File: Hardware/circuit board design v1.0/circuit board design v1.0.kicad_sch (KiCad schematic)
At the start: 0 parts

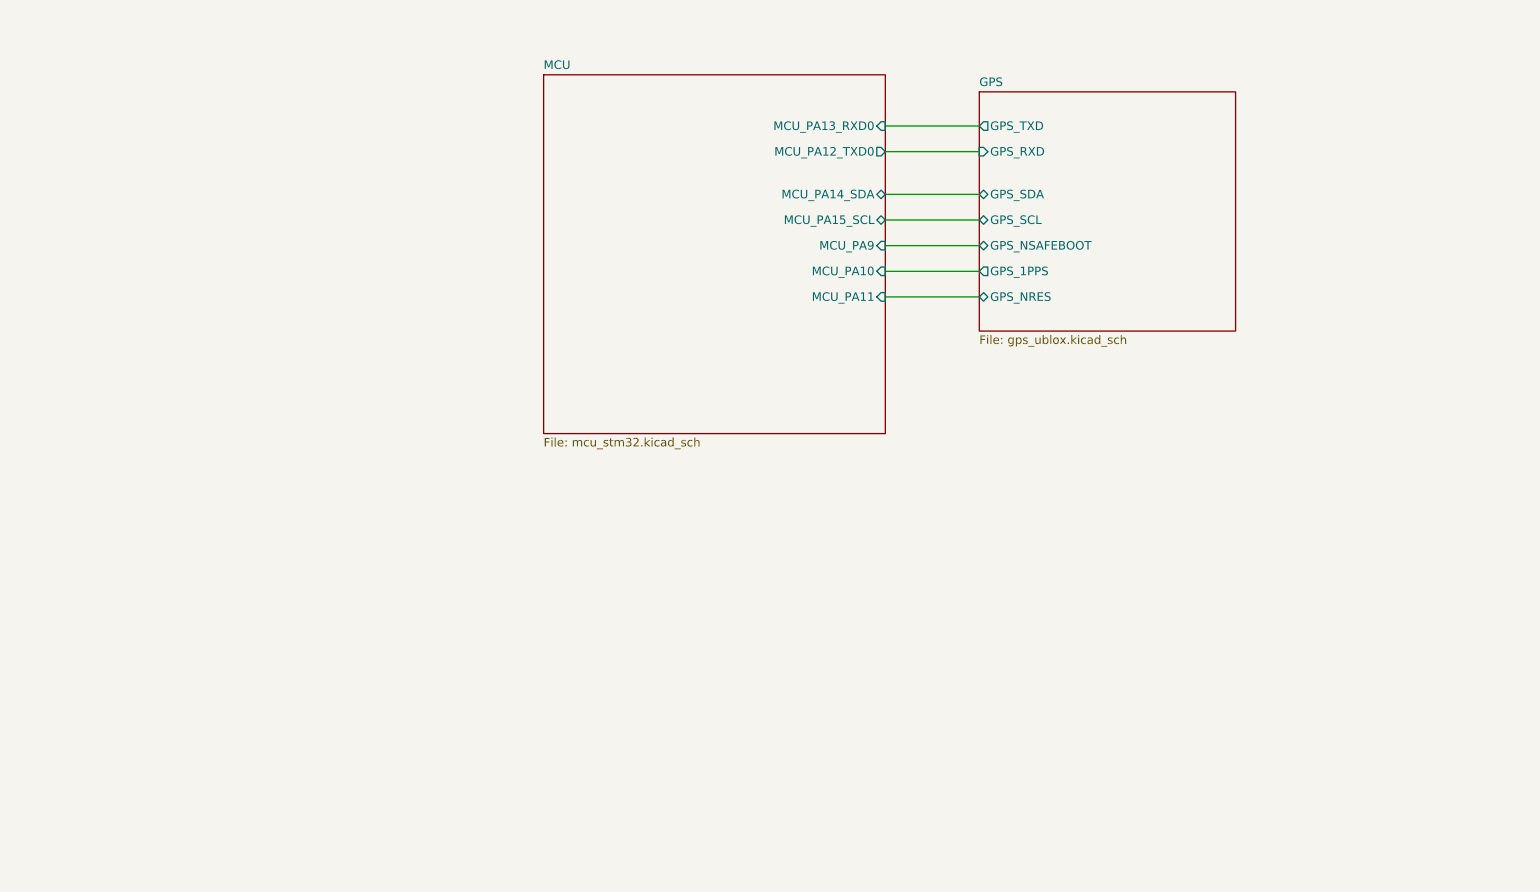
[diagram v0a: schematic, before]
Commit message: Added new diagram and symbol library
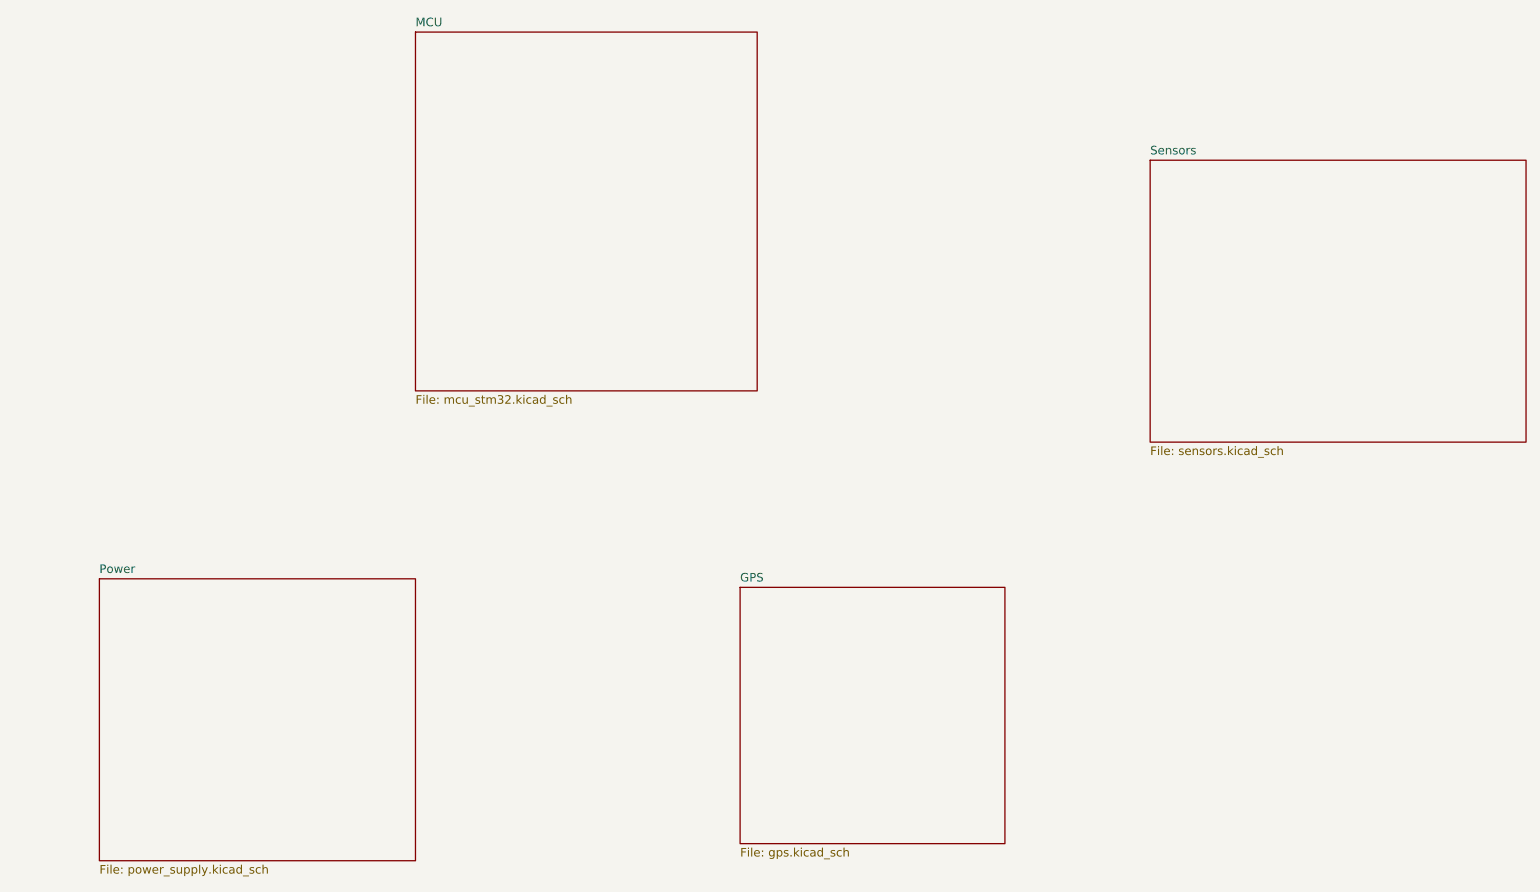
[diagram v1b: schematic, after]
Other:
- added sheet Power (power_supply.kicad_sch)
- added sheet Sensors (sensors.kicad_sch)
- sheet GPS: file gps_ublox.kicad_sch -> gps.kicad_sch
- sheet GPS ports: added none; removed GPS_1PPS, GPS_NRES, GPS_NSAFEBOOT, GPS_RXD, GPS_SCL, GPS_SDA, GPS_TXD
- sheet MCU ports: added none; removed MCU_PA10, MCU_PA11, MCU_PA12_TXD0, MCU_PA13_RXD0, MCU_PA14_SDA, MCU_PA15_SCL, MCU_PA9
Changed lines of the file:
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@@
 (kicad_sch (version 20211123) (generator eeschema)
   (paper "A4")
-  (wire (pts (xy 161.29 50.8) (xy 175.26 50.8))
-    (stroke (width 0) (type default) (color 0 0 0 0))
-  )
-  (wire (pts (xy 161.29 60.96) (xy 175.26 60.96))
-    (stroke (width 0) (type default) (color 0 0 0 0))
-  )
-  (wire (pts (xy 161.29 68.58) (xy 175.26 68.58))
-    (stroke (width 0) (type default) (color 0 0 0 0))
-  )
-  (wire (pts (xy 161.29 72.39) (xy 175.26 72.39))
-    (stroke (width 0) (type default) (color 0 0 0 0))
-  )
-  (wire (pts (xy 161.29 57.15) (xy 175.26 57.15))
-    (stroke (width 0) (type default) (color 0 0 0 0))
-  )
-  (wire (pts (xy 161.29 46.99) (xy 175.26 46.99))
-    (stroke (width 0) (type default) (color 0 0 0 0))
-  )
-  (wire (pts (xy 161.29 64.77) (xy 175.26 64.77))
-    (stroke (width 0) (type default) (color 0 0 0 0))
-  )
-  (sheet (at 175.26 41.91) (size 38.1 35.56) (fields_autoplaced)
+  (sheet (at 200.66 52.07) (size 55.88 41.91) (fields_autoplaced)
     (stroke (width 0.1524) (type solid) (color 0 0 0 0))
     (fill (color 0 0 0 0.0000))
-    (property "Sheet name" "GPS" (id 0) (at 175.26 41.1984 0)
+    (property "Sheet name" "Sensors" (id 0) (at 200.66 51.3584 0)
       (effects (font (size 1.27 1.27)) (justify left bottom))
     )
-    (property "Sheet file" "gps_ublox.kicad_sch" (id 1) (at 175.26 78.0546 0)
+    (property "Sheet file" "sensors.kicad_sch" (id 1) (at 200.66 94.5646 0)
       (effects (font (size 1.27 1.27)) (justify left top))
     )
-    (pin "GPS_1PPS" output (at 175.26 68.58 180)
-      (effects (font (size 1.27 1.27)) (justify left))
+  )
+  (sheet (at 44.45 114.3) (size 46.99 41.91) (fields_autoplaced)
+    (stroke (width 0.1524) (type solid) (color 0 0 0 0))
+    (fill (color 0 0 0 0.0000))
+    (property "Sheet name" "Power" (id 0) (at 44.45 113.5884 0)
+      (effects (font (size 1.27 1.27)) (justify left bottom))
     )
-    (pin "GPS_RXD" input (at 175.26 50.8 180)
-      (effects (font (size 1.27 1.27)) (justify left))
-    )
-    (pin "GPS_SDA" bidirectional (at 175.26 57.15 180)
-      (effects (font (size 1.27 1.27)) (justify left))
-    )
-    (pin "GPS_SCL" bidirectional (at 175.26 60.96 180)
-      (effects (font (size 1.27 1.27)) (justify left))
-    )
-    (pin "GPS_TXD" output (at 175.26 46.99 180)
-      (effects (font (size 1.27 1.27)) (justify left))
-    )
-    (pin "GPS_NRES" bidirectional (at 175.26 72.39 180)
-      (effects (font (size 1.27 1.27)) (justify left))
-    )
-    (pin "GPS_NSAFEBOOT" bidirectional (at 175.26 64.77 180)
-      (effects (font (size 1.27 1.27)) (justify left))
+    (property "Sheet file" "power_supply.kicad_sch" (id 1) (at 44.45 156.7946 0)
+      (effects (font (size 1.27 1.27)) (justify left top))
     )
   )
-  (sheet (at 110.49 39.37) (size 50.8 53.34) (fields_autoplaced)
+  (sheet (at 139.7 115.57) (size 39.37 38.1) (fields_autoplaced)
     (stroke (width 0.1524) (type solid) (color 0 0 0 0))
     (fill (color 0 0 0 0.0000))
-    (property "Sheet name" "MCU" (id 0) (at 110.49 38.6584 0)
+    (property "Sheet name" "GPS" (id 0) (at 139.7 114.8584 0)
       (effects (font (size 1.27 1.27)) (justify left bottom))
     )
-    (property "Sheet file" "mcu_stm32.kicad_sch" (id 1) (at 110.49 93.2946 0)
+    (property "Sheet file" "gps.kicad_sch" (id 1) (at 139.7 154.2546 0)
       (effects (font (size 1.27 1.27)) (justify left top))
     )
-    (pin "MCU_PA14_SDA" bidirectional (at 161.29 57.15 0)
-      (effects (font (size 1.27 1.27)) (justify right))
+  )
+  (sheet (at 91.44 33.02) (size 50.8 53.34) (fields_autoplaced)
+    (stroke (width 0.1524) (type solid) (color 0 0 0 0))
+    (fill (color 0 0 0 0.0000))
+    (property "Sheet name" "MCU" (id 0) (at 91.44 32.3084 0)
+      (effects (font (size 1.27 1.27)) (justify left bottom))
     )
-    (pin "MCU_PA15_SCL" bidirectional (at 161.29 60.96 0)
-      (effects (font (size 1.27 1.27)) (justify right))
-    )
-    (pin "MCU_PA9" input (at 161.29 64.77 0)
-      (effects (font (size 1.27 1.27)) (justify right))
-    )
-    (pin "MCU_PA11" input (at 161.29 72.39 0)
-      (effects (font (size 1.27 1.27)) (justify right))
-    )
-    (pin "MCU_PA10" input (at 161.29 68.58 0)
-      (effects (font (size 1.27 1.27)) (justify right))
-    )
-    (pin "MCU_PA13_RXD0" input (at 161.29 46.99 0)
-      (effects (font (size 1.27 1.27)) (justify right))
-    )
-    (pin "MCU_PA12_TXD0" output (at 161.29 50.8 0)
-      (effects (font (size 1.27 1.27)) (justify right))
+    (property "Sheet file" "mcu_stm32.kicad_sch" (id 1) (at 91.44 86.9446 0)
+      (effects (font (size 1.27 1.27)) (justify left top))
     )
   )
@@
     (path "/" (page "1"))
     (path "/b2e7fea0-7ba9-48b0-990f-5c369d704fdf" (page "3"))
-    (path "/8e330075-8519-4590-9420-bffcbb9dc43b" (page "3"))
+    (path "/0e7a8511-bb07-4cdf-8fc9-61e0cb55f4d9" (page "3"))
+    (path "/5a4d8c5a-da32-47cd-8dfd-858fccee0cc7" (page "5"))
+    (path "/91cf0010-9ee0-4eb5-a57e-e0ac00755c97" (page "5"))
   )
   (symbol_instances
-    (path "/8e330075-8519-4590-9420-bffcbb9dc43b/d87f6ea3-c060-42a5-97a0-420a1c921045"
-      (reference "#PWR0101") (unit 1) (value "GND") (footprint "")
+    (path "/b2e7fea0-7ba9-48b0-990f-5c369d704fdf/4d468306-9ceb-4a69-b007-fa8ae388cbdd"
+      (reference "U?") (unit 1) (value "SDR08540M3-01") (footprint "")
     )
-    (path "/8e330075-8519-4590-9420-bffcbb9dc43b/57c20c7f-3f98-4653-9bfc-208f45e6923e"
-      (reference "#PWR0102") (unit 1) (value "GND") (footprint "")
+    (path "/b2e7fea0-7ba9-48b0-990f-5c369d704fdf/63f188be-8ad2-4239-b8d8-d5822711dd1d"
+      (reference "U?") (unit 1) (value "W25Q64JVSS") (footprint "Package_SO:SOIC-8_5.23x5.23mm_P1.27mm")
     )
-    (path "/8e330075-8519-4590-9420-bffcbb9dc43b/1810412a-ed5b-4bb4-a68f-47225649fa88"
-      (reference "#PWR0103") (unit 1) (value "GND") (footprint "")
+    (path "/91cf0010-9ee0-4eb5-a57e-e0ac00755c97/712bd423-afa1-4088-9564-2d6002f8925c"
+      (reference "U?") (unit 1) (value "L80-R") (footprint "RF_GPS:Quectel_L80-R")
     )
-    (path "/8e330075-8519-4590-9420-bffcbb9dc43b/7d81221c-e9ab-48af-b7d7-1815223804b6"
-      (reference "#PWR0104") (unit 1) (value "+3.3V") (footprint "")
+    (path "/0e7a8511-bb07-4cdf-8fc9-61e0cb55f4d9/ed71ed88-8cab-4422-86f8-4a2a4f8c82ab"
+      (reference "U?") (unit 1) (value "BME280") (footprint "Package_LGA:Bosch_LGA-8_2.5x2.5mm_P0.65mm_ClockwisePinNumbering")
     )
-    (path "/8e330075-8519-4590-9420-bffcbb9dc43b/787599bc-6028-438c-b2ca-5c1b4553be29"
-      (reference "#PWR0105") (unit 1) (value "GND") (footprint "")
-    )
-    (path "/8e330075-8519-4590-9420-bffcbb9dc43b/b16e5f76-da13-4db4-9b9e-1edca3725b44"
-      (reference "C8") (unit 1) (value "10nF") (footprint "")
-    )
-    (path "/8e330075-8519-4590-9420-bffcbb9dc43b/84f3c0dc-174b-42b2-b519-5c117804d11a"
-      (reference "C11") (unit 1) (value "100nF") (footprint "")
-    )
-    (path "/8e330075-8519-4590-9420-bffcbb9dc43b/9acf1ab0-855e-486d-a4e4-205d12488aa1"
-      (reference "C12") (unit 1) (value "10uF") (footprint "")
-    )
-    (path "/8e330075-8519-4590-9420-bffcbb9dc43b/644fd1d5-0dd9-4b76-a36d-ddb1fb52a7b6"
-      (reference "J1") (unit 1) (value "Conn_Coaxial") (footprint "")
-    )
-    (path "/8e330075-8519-4590-9420-bffcbb9dc43b/ebba5298-8112-4586-9cf1-e4f498da6ef8"
-      (reference "L2") (unit 1) (value "27nH") (footprint "")
-    )
-    (path "/8e330075-8519-4590-9420-bffcbb9dc43b/a2c4cb1e-ae3b-4df8-bf5e-ecdaac4fa95d"
-      (reference "R2") (unit 1) (value "10 Ohm") (footprint "")
-    )
-    (path "/b2e7fea0-7ba9-48b0-990f-5c369d704fdf/14325fd2-ca01-4d4d-a6ab-b0b5f24fcdf3"
-      (reference "U1") (unit 1) (value "STM32F303RCTx") (footprint "Package_QFP:LQFP-64_10x10mm_P0.5mm")
-    )
-    (path "/8e330075-8519-4590-9420-bffcbb9dc43b/27cbbdd0-0532-474f-b527-ac1257ddb455"
-      (reference "U2") (unit 1) (value "MAX-M8Q") (footprint "RF_GPS:ublox_MAX")
+    (path "/b2e7fea0-7ba9-48b0-990f-5c369d704fdf/ede98502-4efb-410a-b6ea-935bd2230c54"
+      (reference "U?") (unit 1) (value "STM32F446RETx") (footprint "Package_QFP:LQFP-64_10x10mm_P0.5mm")
     )
   )

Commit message: Changes on 14/02/2023
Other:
- sheet Sensors ports: added SCL, SDA; removed none
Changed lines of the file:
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@@
       (effects (font (size 1.27 1.27)) (justify left top))
+    )
+    (pin "SCL" bidirectional (at 200.66 67.31 180)
+      (effects (font (size 1.27 1.27)) (justify left))
+    )
+    (pin "SDA" bidirectional (at 200.66 72.39 180)
+      (effects (font (size 1.27 1.27)) (justify left))
     )
   )
@@
       (reference "#PWR?") (unit 1) (value "VBUS") (footprint "")
     )
+    (path "/0e7a8511-bb07-4cdf-8fc9-61e0cb55f4d9/0ed6d568-4ff0-4706-981e-644385d4eeaf"
+      (reference "#PWR?") (unit 1) (value "+3.3V") (footprint "")
+    )
     (path "/5a4d8c5a-da32-47cd-8dfd-858fccee0cc7/1fe0f843-f74c-424a-ab04-ee1e9d27a10f"
       (reference "#PWR?") (unit 1) (value "+3.3V") (footprint "")
@@
       (reference "#PWR?") (unit 1) (value "GND") (footprint "")
     )
+    (path "/0e7a8511-bb07-4cdf-8fc9-61e0cb55f4d9/275e6250-f94b-40a1-8230-c43fb0e7da95"
+      (reference "#PWR?") (unit 1) (value "+3.3VA") (footprint "")
+    )
     (path "/5a4d8c5a-da32-47cd-8dfd-858fccee0cc7/344f6c00-7c26-47ec-979d-852a4539b089"
       (reference "#PWR?") (unit 1) (value "GND") (footprint "")
     )
     (path "/5a4d8c5a-da32-47cd-8dfd-858fccee0cc7/3975a517-85d0-4096-b602-472abd03ef7e"
+      (reference "#PWR?") (unit 1) (value "GND") (footprint "")
+    )
+    (path "/0e7a8511-bb07-4cdf-8fc9-61e0cb55f4d9/443886d2-fb55-4fd8-8135-83f1c746e9db"
       (reference "#PWR?") (unit 1) (value "GND") (footprint "")
     )
@@
       (reference "#PWR?") (unit 1) (value "GND") (footprint "")
     )
+    (path "/0e7a8511-bb07-4cdf-8fc9-61e0cb55f4d9/75c84ad0-9e28-4279-b064-0beebeaa0453"
+      (reference "#PWR?") (unit 1) (value "GND") (footprint "")
+    )

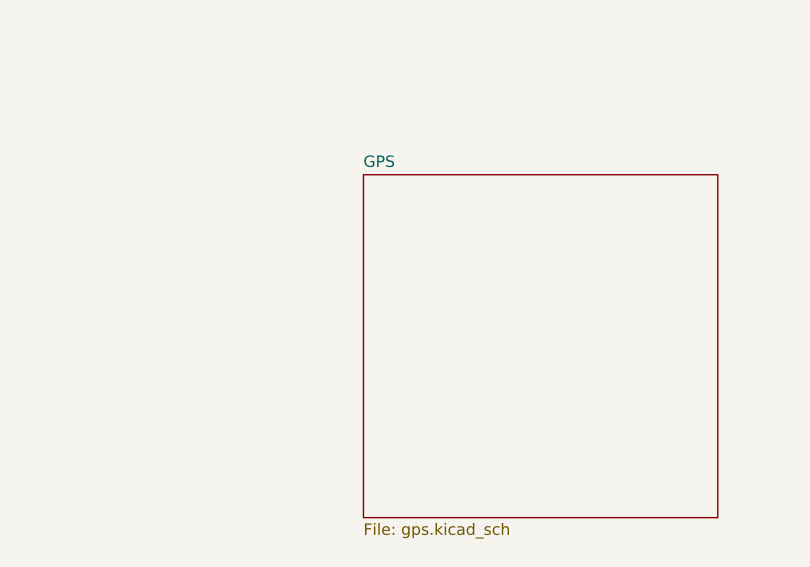
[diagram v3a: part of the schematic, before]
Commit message: BMI088 schematic
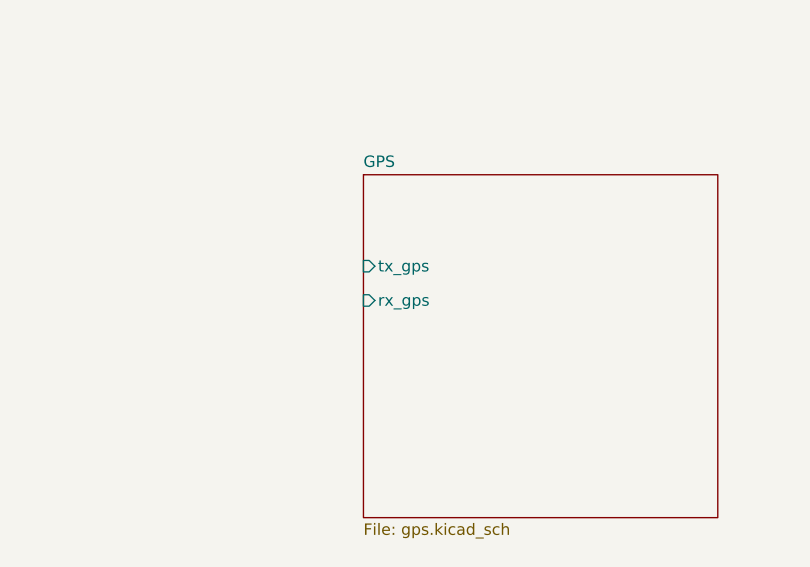
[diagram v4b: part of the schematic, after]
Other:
- sheet GPS ports: added rx_gps, tx_gps; removed none
